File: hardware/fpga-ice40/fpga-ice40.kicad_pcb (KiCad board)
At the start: 4 copper layers, 53.3 x 48.6 mm, 94 parts, among them J1 Conn_01x03, J2 MicroSD_Molex_1040310811, J3 FTSH-105-01-L-DV-K, J4 FTSH-105-01-L-DV-K, J5 USB_B_Micro, J6 Conn_02x20_Odd_Even, Q1 2N7002H-7, U1 iCE40HX4K-TQ144, U10 MC74HC1G08DTT1G, U2 AZ1117-3.3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

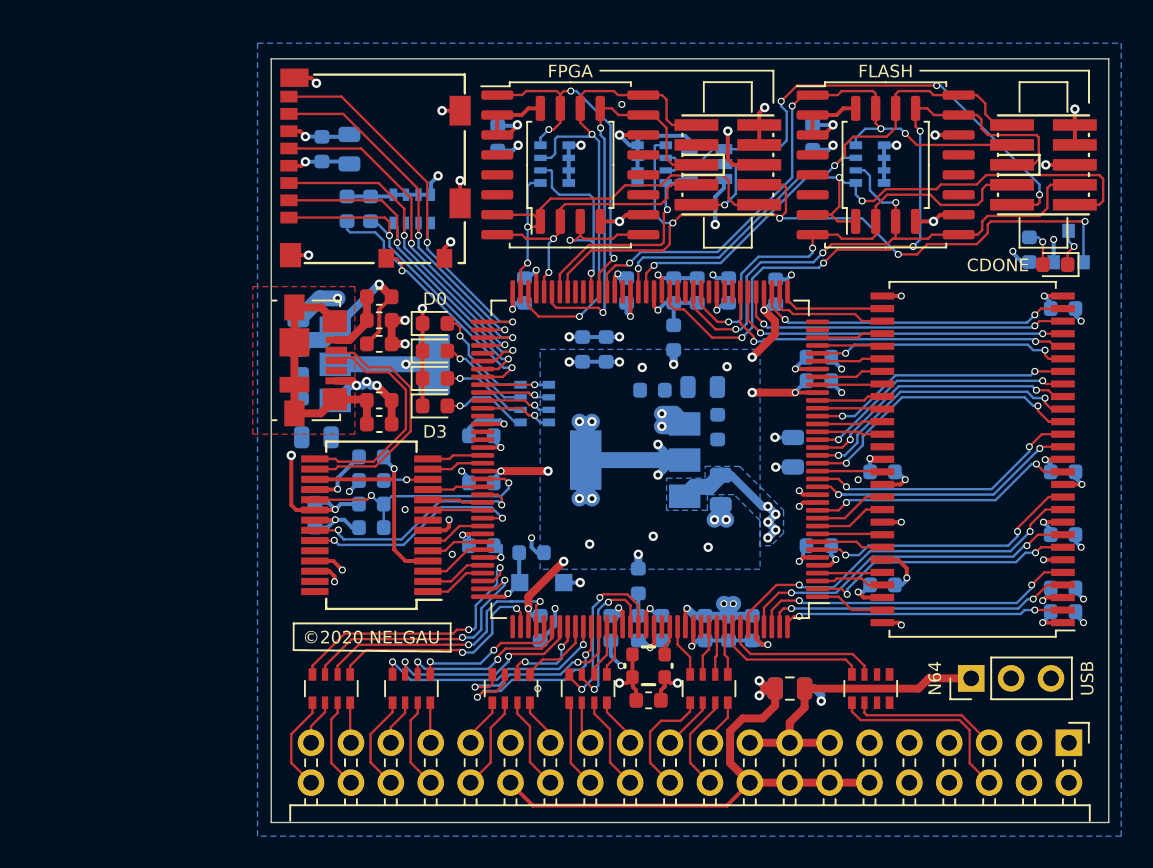
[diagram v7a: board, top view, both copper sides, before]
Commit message: Fix mechanical issue by moving USB connector to top of board
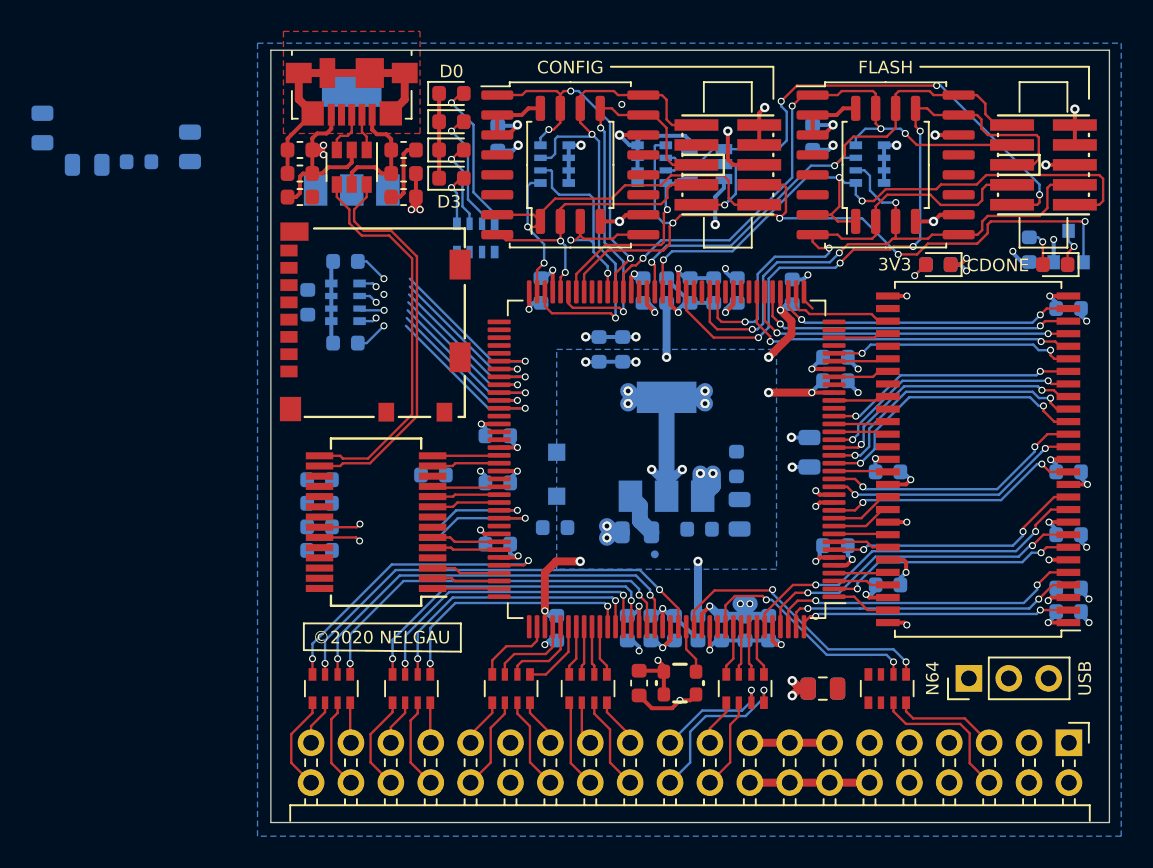
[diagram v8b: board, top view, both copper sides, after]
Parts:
- added C48: 100n, Capacitor_SMD:C_0603_1608Metric, F.Cu at (144.3, 78.3)
- added D7: Green, LED_SMD:LED_0603_1608Metric, F.Cu at (178.3, 82.6)
- added R13: 1k, Resistor_SMD:R_0603_1608Metric, B.Cu at (178.3, 82.6)
- added U11: USBLC6-2SC6, Package_TO_SOT_SMD:SOT-23-6, F.Cu at (141.0, 76.4)
- C18: value 10n -> 100n
- C19: moved to F.Cu
- C21: moved to B.Cu
- moved C19 20.3 mm to (137.7, 78.3), turned to 180 degrees
- moved C2 20.2 mm to (130.7, 75.1), turned to 90 degrees
- moved C16 19.6 mm to (121.3, 73.9)
- moved R2 18.2 mm to (137.7, 75.3)
- moved R9 17.7 mm to (127.5, 76.0), turned to 0 degrees
- moved J5 17.3 mm to (141.0, 71.6), turned to 180 degrees
- moved C1 17.2 mm to (124.2, 76.2), turned to 180 degrees
- moved C20 15.3 mm to (137.7, 76.8)
- moved D3 14.7 mm to (147.3, 71.7)
- moved D4 14.6 mm to (147.3, 73.5)
- moved D5 14.6 mm to (147.3, 75.3)
- moved D6 14.5 mm to (147.3, 77.1)
- moved U2 14.4 mm to (141.0, 74.7), turned to 90 degrees
- moved R11 11.2 mm to (148.9, 80.9), turned to 270 degrees
- moved C21 10.8 mm to (138.9, 97.8), turned to 180 degrees
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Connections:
- J5 pad 2: USB_D- -> xUSB_D-
- J5 pad 3: USB_D+ -> xUSB_D+
- R1 pad 2: SD_DAT2 -> SD_DAT1
- RN3 pad 1: SD_DAT1 -> SD_DAT0
- RN3 pad 2: SD_DAT0 -> SD_CMD
- RN3 pad 3: SD_CMD -> SD_DAT3
- RN3 pad 4: SD_DAT3 -> SD_DAT2
- RN7 pad 1: N64_AD9 -> N64_AD7
- RN7 pad 2: N64_AD6 -> N64_AD8
- RN7 pad 3: N64_AD8 -> N64_AD6
- RN7 pad 4: N64_AD7 -> N64_AD9
- RN7 pad 5: N64_AD7_IC -> N64_AD9_IC
- RN7 pad 6: N64_AD8_IC -> N64_AD6_IC
- RN7 pad 7: N64_AD6_IC -> N64_AD8_IC
- RN7 pad 8: N64_AD9_IC -> N64_AD7_IC
- RN9 pad 1: N64_OS_EVENTn -> Net-(RN9-Pad1)
- RN9 pad 2: N64_COLD_RESETn -> Net-(RN9-Pad2)
- RN9 pad 3: Net-(RN9-Pad3) -> N64_OS_EVENTn
- RN9 pad 4: Net-(RN9-Pad4) -> N64_COLD_RESETn
- RN9 pad 5: Net-(RN9-Pad5) -> N64_COLD_RESETn_IC
- RN9 pad 6: Net-(RN9-Pad6) -> N64_OS_EVENTn_IC
- RN9 pad 7: N64_COLD_RESETn_IC -> Net-(RN9-Pad7)
- RN9 pad 8: N64_OS_EVENTn_IC -> Net-(RN9-Pad8)
- U1 pad 101: FIFO_D1 -> FIFO_D7
- U1 pad 102: FIFO_D2 -> FIFO_D1
- U1 pad 104: FIFO_D4 -> N64_AD15_IC
- U1 pad 105: FIFO_D0 -> FIFO_D2
- U1 pad 106: N64_AD15_IC -> FIFO_D4
- U1 pad 107: N64_AD0_IC -> FIFO_D0
- U1 pad 110: N64_AD1_IC -> N64_ALE_L_IC
- U1 pad 112: N64_AD14_IC -> N64_WRITEn_IC
- U1 pad 113: N64_AD3_IC -> N64_READn_IC
- U1 pad 114: N64_AD12_IC -> N64_ALE_H_IC
- U1 pad 115: N64_AD2_IC -> N64_AD11_IC
- U1 pad 116: N64_READn_IC -> N64_AD4_IC
- U1 pad 117: N64_ALE_H_IC -> N64_AD10_IC
- U1 pad 118: N64_AD13_IC -> N64_AD5_IC
- U1 pad 119: N64_WRITEn_IC -> N64_AD3_IC
- U1 pad 120: N64_ALE_L_IC -> N64_AD12_IC
- U1 pad 121: N64_AD10_IC -> N64_AD2_IC
- U1 pad 122: N64_AD5_IC -> N64_AD13_IC
- U1 pad 124: N64_AD4_IC -> N64_AD1_IC
- U1 pad 125: N64_AD11_IC -> N64_AD14_IC
- U1 pad 128: Net-(U1-Pad128) -> N64_AD0_IC
- U1 pad 130: N64_AD9_IC -> N64_COLD_RESETn_IC
- U1 pad 134: N64_AD6_IC -> N64_OS_EVENTn_IC
- U1 pad 135: N64_AD8_IC -> N64_AD7_IC
- U1 pad 136: N64_AD7_IC -> N64_AD8_IC
- U1 pad 137: N64_OS_EVENTn_IC -> N64_AD6_IC
- U1 pad 138: N64_COLD_RESETn_IC -> N64_AD9_IC
- U1 pad 73: SD_DAT1 -> LED_D0
- U1 pad 74: SD_DAT0 -> LED_D1
- U1 pad 75: SD_CLK -> LED_D2
- U1 pad 76: SD_CMD -> LED_D3
- U1 pad 78: SD_DAT3 -> SD_DAT1
- U1 pad 79: SD_DAT2 -> SD_DAT0
- U1 pad 80: SD_CD -> SD_CLK
- U1 pad 81: LED_D0 -> SD_CMD
- U1 pad 82: LED_D1 -> SD_DAT3
- U1 pad 83: LED_D2 -> SD_DAT2
- U1 pad 84: LED_D3 -> SD_CD
- U1 pad 95: FIFO_TXEn -> FIFO_D6
- U1 pad 96: FIFO_D6 -> FIFO_D5
- U1 pad 97: FIFO_D5 -> FIFO_TXEn
- U1 pad 99: FIFO_D7 -> Net-(U1-Pad99)
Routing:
- net GND: track 164.0 -> 111.9 mm, vias 69 -> 51
- net USB_5V: track 34.1 -> 4.28 mm, vias 3 -> 0
- net USB_DETn: track 16.7 -> 0.00 mm, vias 2 -> 0
- net N64_3V3: track 19.8 -> 5.08 mm
- net /Interface_USB/USB_VIO: track 13.7 -> 0.00 mm, vias 1 -> 0
- net P3V3: track 109.6 -> 96.6 mm, vias 38 -> 30
- net SD_DAT1: track 25.9 -> 13.3 mm
- net SD_DAT0: track 23.8 -> 11.3 mm
- net N64_AD0_IC: track 16.9 -> 28.7 mm
- net SD_CLK: track 23.0 -> 11.2 mm
- net SD_DAT2: track 22.2 -> 11.5 mm
- net N64_AD1_IC: track 14.8 -> 25.2 mm
- net SD_CMD: track 21.7 -> 11.5 mm
- net USB_D+: track 14.6 -> 24.8 mm
- net SD_DAT3: track 23.0 -> 13.0 mm
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- removed copper zone on B.Cu, net P3V3
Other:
- board size 53.3 x 48.6 mm -> 53.4 x 49.2 mm
- board text added: "3V3"
- board text added: "CONFIG"
- board text removed: "FPGA"
